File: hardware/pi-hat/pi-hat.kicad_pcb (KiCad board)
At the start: 2 copper layers, 65 x 56 mm, 98 parts, among them J1 PWR_IN, J10 6-8, J11 LED0, J12 LED1, J13 KLPX-0848A-2-B, J14 KLPX-0848A-2-R, J2 A-F, J3 40HAT, J4 G-M, J5 N-Q, J6 PANEL_PWR, J7 PANEL_CTL, J8 2-5, J9 WP, Q1 DMG2305UX, Q2 DMMT5401, Q3 DMN6075S, Q4 DMP4065S, Q5 DMN6075S, U1 CAT24C32, U10 L78L33_SOT89, U11 L78L33_SOT89, U12 PCM5122PW, U13 TSR_2-2450, U14 TSR_2-2450, U2 CM1293A, U3 CM1293A, U4 CM1293A, U5 CM1293A, U6 CM1293A, U7 CM1293A, U8 MCP23S17_SO, U9 MCP23S17_SO

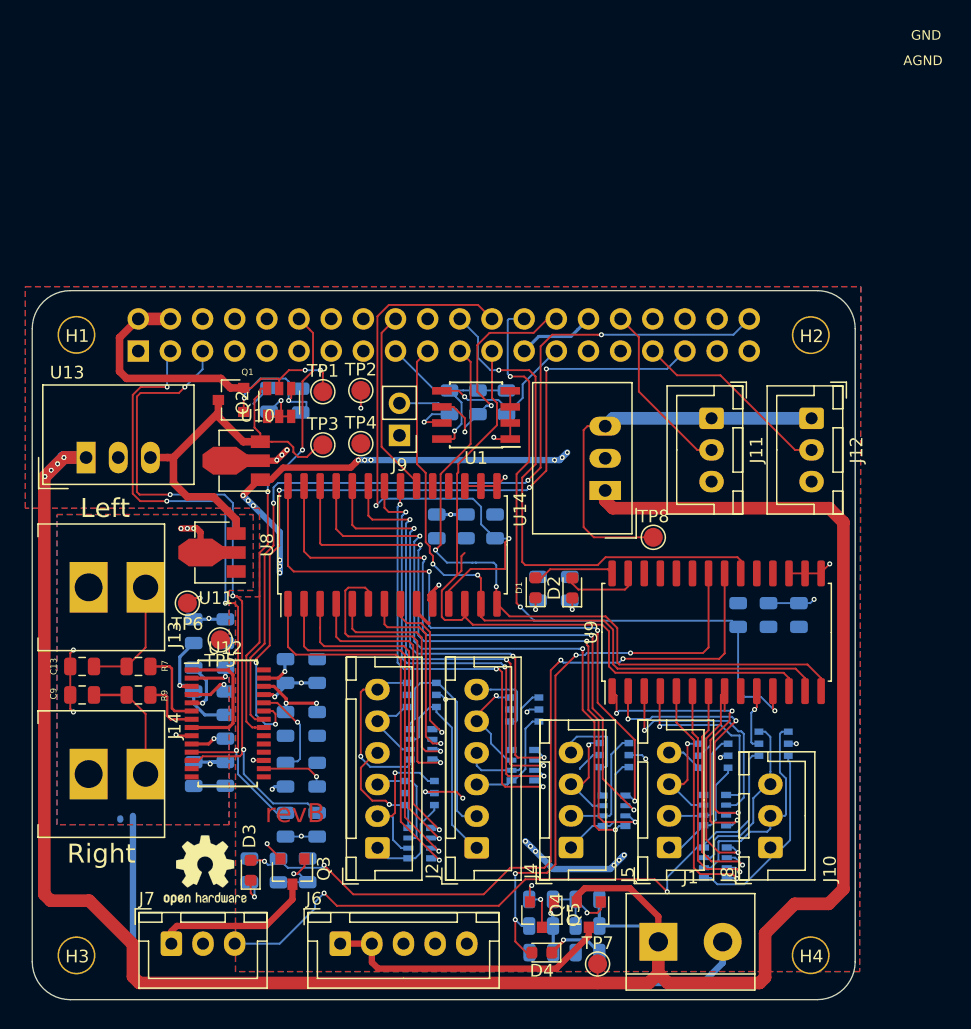
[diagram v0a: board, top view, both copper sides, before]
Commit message: final routing and silkscreen cleanup
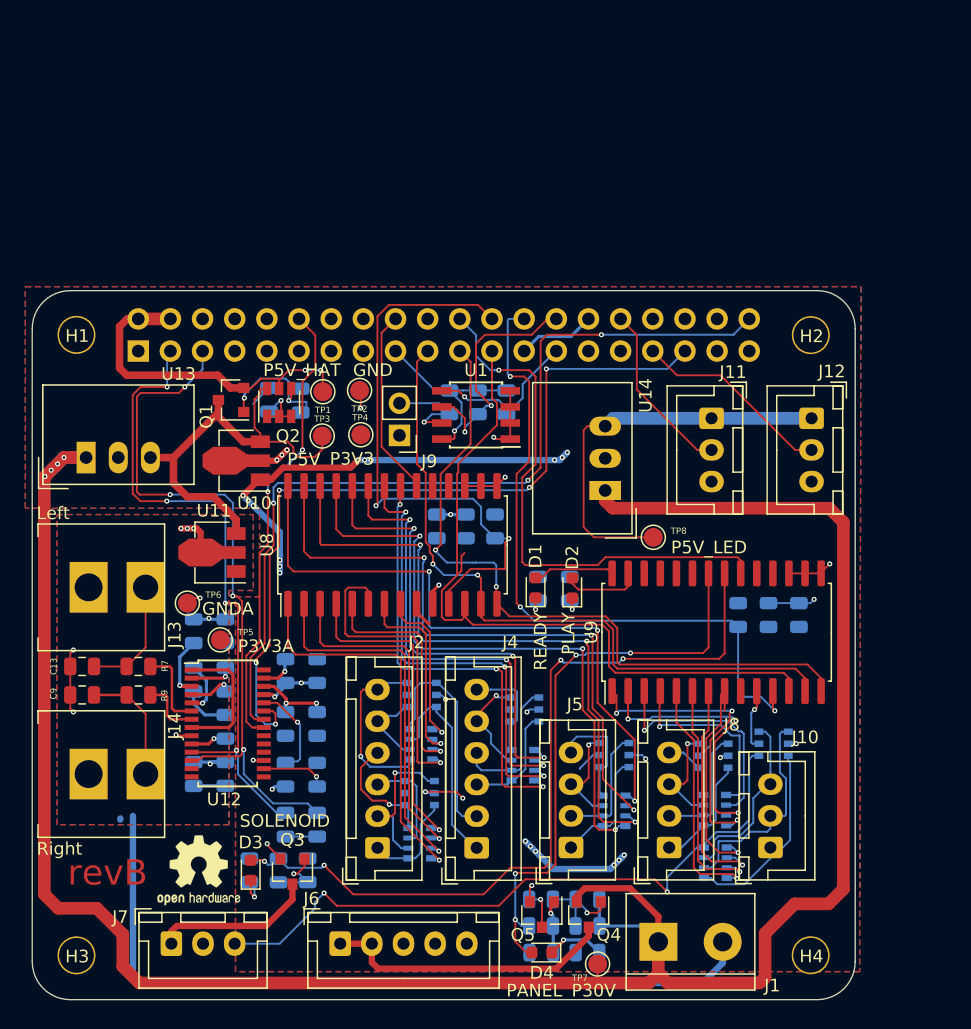
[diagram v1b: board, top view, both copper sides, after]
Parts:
- moved TP3 0.70 mm to (101.5, 72.3)
- moved TP4 0.70 mm to (104.5, 72.2)
- moved OSHW1 0.50 mm to (91.7, 106.6)
- moved TP2 0.10 mm to (104.4, 68.7)
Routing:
- net /P5V: track 32.1 -> 33.6 mm
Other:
- board text removed: "AGND"
- board text removed: "GND"
- board text removed: "P3V3"
- board text removed: "P3V3A"
